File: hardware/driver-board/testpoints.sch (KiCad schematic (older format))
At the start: 23 parts

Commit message: Board layout on work
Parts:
- added TP24, TP25: TestPoint, TestPoint:TestPoint_Pad_D0.5mm, symbol Connector:TestPoint
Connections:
- new net FTRES: TP24.1
- new net IRQ: TP25.1
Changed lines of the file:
@@
 Text GLabel 6300 4350 2    50   UnSpc ~ 0
 AUDIO
+$Comp
+L Connector:TestPoint TP24
+U 1 1 5F0486C1
+P 6300 4500
+F 0 "TP24" V 6300 4850 50  0000 C CNN
+F 1 "TestPoint" V 6404 4572 50  0001 C CNN
+F 2 "TestPoint:TestPoint_Pad_D0.5mm" H 6500 4500 50  0001 C CNN
+F 3 "~" H 6500 4500 50  0001 C CNN
+	1    6300 4500
+	0    -1   -1   0
+$EndComp
+Text GLabel 6300 4500 2    50   UnSpc ~ 0
+FTRES
+$Comp
+L Connector:TestPoint TP25
+U 1 1 5F048FDB
+P 6300 4650
+F 0 "TP25" V 6300 5000 50  0000 C CNN
+F 1 "TestPoint" V 6404 4722 50  0001 C CNN
+F 2 "TestPoint:TestPoint_Pad_D0.5mm" H 6500 4650 50  0001 C CNN
+F 3 "~" H 6500 4650 50  0001 C CNN
+	1    6300 4650
+	0    -1   -1   0
+$EndComp
+Text GLabel 6300 4650 2    50   UnSpc ~ 0
+IRQ
 $EndSCHEMATC

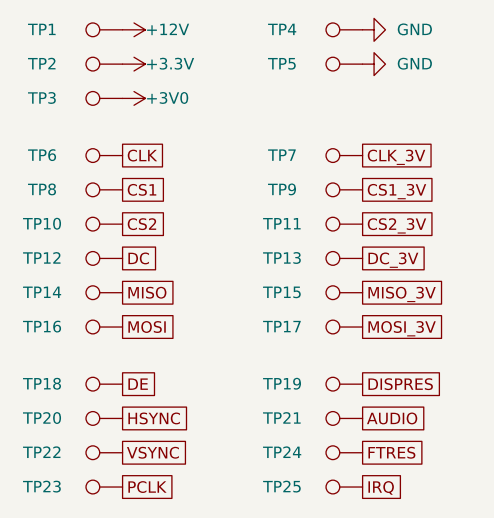
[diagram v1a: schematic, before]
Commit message: Adapt new SPI signal names from OSHWA
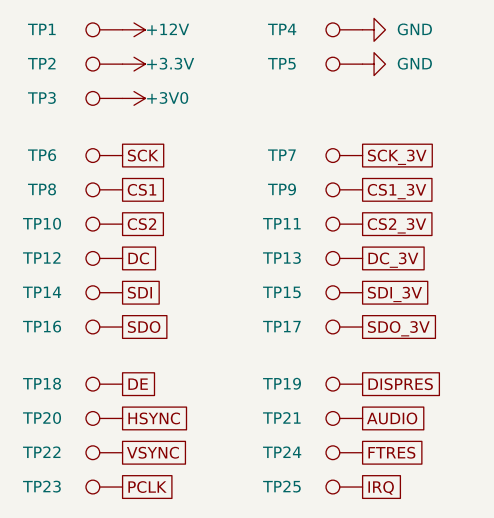
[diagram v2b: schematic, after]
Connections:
- net CLK renamed SCK
- net CLK_3V renamed SCK_3V
- net MISO renamed SDI
- net MISO_3V renamed SDI_3V
- net MOSI renamed SDO
- net MOSI_3V renamed SDO_3V
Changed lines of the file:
@@
 $EndComp
 Text GLabel 5250 3200 2    50   UnSpc ~ 0
-CLK
+SCK
 $Comp
 L Connector:TestPoint TP8
@@
 $EndComp
 Text GLabel 5250 3800 2    50   UnSpc ~ 0
-MISO
+SDI
 $Comp
 L Connector:TestPoint TP16
@@
 $EndComp
 Text GLabel 5250 3950 2    50   UnSpc ~ 0
-MOSI
+SDO
 $Comp
 L Connector:TestPoint TP7
@@
 $EndComp
 Text GLabel 6300 3200 2    50   UnSpc ~ 0
-CLK_3V
+SCK_3V
 $Comp
 L Connector:TestPoint TP9
@@
 $EndComp
 Text GLabel 6300 3800 2    50   UnSpc ~ 0
-MISO_3V
+SDI_3V
 $Comp
 L Connector:TestPoint TP17
@@
 $EndComp
 Text GLabel 6300 3950 2    50   UnSpc ~ 0
-MOSI_3V
+SDO_3V
 $Comp
 L Connector:TestPoint TP18
